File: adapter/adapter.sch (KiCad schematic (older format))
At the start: 6 parts, among them J1 Conn_01x04_Male, J2 RJ45, J3 Conn_01x02_Male

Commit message: Add some adapter and interconnect pics
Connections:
- net GND: now also J1.4 (Pin_4); no longer J1.1 (Pin_1)
- net A: now reaches J1.2 (Pin_2), J2.1
- net B: now reaches J1.3 (Pin_3), J2.2
- net A/GND: now reaches J2.7, JP2.1 (A)
- net B/VCC: now reaches J2.8, JP1.1 (A)
- net at JP3.1 (A): now also J1.1 (Pin_1); no longer J1.4 (Pin_4)
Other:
- moved on the sheet: J2, JP3
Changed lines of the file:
@@
 Comment9 ""
 $EndDescr
-Wire Wire Line
-	3550 4700 5275 4700
-Wire Wire Line
-	4625 4300 3550 4300
-Wire Wire Line
-	4525 4600 3550 4600
-Wire Wire Line
-	4625 4500 3550 4500
+Connection ~ 4175 4400
+Connection ~ 4525 4600
+Connection ~ 4625 3975
+Connection ~ 4625 4300
+Wire Wire Line
+	2750 4100 3775 4100
+Wire Wire Line
+	2750 4200 3775 4200
+Wire Wire Line
+	2750 4700 5275 4700
+Wire Wire Line
+	2750 4800 5375 4800
+Wire Wire Line
+	3775 4100 3775 3975
+Wire Wire Line
+	3975 3075 5200 3075
+Wire Wire Line
+	4175 3975 4625 3975
+Wire Wire Line
+	4175 4200 4175 4400
+Wire Wire Line
+	4175 4400 2750 4400
 Wire Wire Line
 	4525 4400 4175 4400
 Wire Wire Line
-	5200 4250 5850 4250
+	4525 4400 4525 4600
+Wire Wire Line
+	4525 4600 2750 4600
+Wire Wire Line
+	4525 4600 4525 4875
+Wire Wire Line
+	4625 3975 4625 4300
+Wire Wire Line
+	4625 4300 2750 4300
+Wire Wire Line
+	4625 4300 4625 4500
+Wire Wire Line
+	4625 4300 5050 4300
+Wire Wire Line
+	4625 4500 2750 4500
+Wire Wire Line
+	5050 4300 5050 3800
+Wire Wire Line
+	5200 3075 5200 3550
+Wire Wire Line
+	5200 4050 5750 4050
+Wire Wire Line
+	5275 4350 5850 4350
+Wire Wire Line
+	5275 4700 5275 4350
+Wire Wire Line
+	5375 4450 5850 4450
 Wire Wire Line
 	5375 4800 5375 4450
 Wire Wire Line
-	5375 4450 5850 4450
-Wire Wire Line
-	5275 4350 5850 4350
-Wire Wire Line
-	5275 4700 5275 4350
+	5650 4250 5650 4550
+Wire Wire Line
+	5750 4050 5750 4550
+Wire Wire Line
+	5750 4550 5850 4550
+Wire Wire Line
+	5850 4250 5650 4250
+Text Notes 2925 4300 2    50   ~ 0
+O
+Text Notes 2925 4400 2    50   ~ 0
+BW
+Text Notes 2925 4500 2    50   ~ 0
+B
+Text Notes 2925 4600 2    50   ~ 0
+OW
+Text Notes 2925 4700 2    50   ~ 0
+G
+Text Notes 2950 4100 2    50   ~ 0
+BR
+Text Notes 2950 4200 2    50   ~ 0
+BRW
+Text Notes 2950 4800 2    50   ~ 0
+GW
+Text Label 3125 4300 2    50   ~ 0
+VCC
+Text Label 3125 4400 2    50   ~ 0
+GND
+Text Label 3125 4500 2    50   ~ 0
+VCC
+Text Label 3125 4600 2    50   ~ 0
+GND
+Text Label 3125 4700 2    50   ~ 0
+B
+Text Label 3125 4800 2    50   ~ 0
+A
+Text Label 3250 4100 2    50   ~ 0
+B{slash}VCC
+Text Label 3250 4200 2    50   ~ 0
+A{slash}GND
+Text Label 5550 4350 2    50   ~ 0
+B
+Text Label 5550 4450 2    50   ~ 0
+A
+$Comp
+L power:VCC #PWR?
+U 1 1 5E309DAF
+P 4625 3975
+F 0 "#PWR?" H 4625 3825 50  0001 C CNN
+F 1 "VCC" H 4640 4148 50  0000 C CNN
+F 2 "" H 4625 3975 50  0001 C CNN
+F 3 "" H 4625 3975 50  0001 C CNN
+	1    4625 3975
+	1    0    0    -1
+$EndComp
+$Comp
+L power:GND #PWR?
+U 1 1 5E310096
+P 3975 3175
+F 0 "#PWR?" H 3975 2925 50  0001 C CNN
+F 1 "GND" H 3980 3002 50  0000 C CNN
+F 2 "" H 3975 3175 50  0001 C CNN
+F 3 "" H 3975 3175 50  0001 C CNN
+	1    3975 3175
+	1    0    0    -1
+$EndComp
+$Comp
+L power:GND #PWR?
+U 1 1 5E30A136
+P 4525 4875
+F 0 "#PWR?" H 4525 4625 50  0001 C CNN
+F 1 "GND" H 4530 4702 50  0000 C CNN
+F 2 "" H 4525 4875 50  0001 C CNN
+F 3 "" H 4525 4875 50  0001 C CNN
+	1    4525 4875
+	1    0    0    -1
+$EndComp
+$Comp
+L power:GND #PWR?
+U 1 1 5E30BC3A
+P 5650 4550
+F 0 "#PWR?" H 5650 4300 50  0001 C CNN
+F 1 "GND" H 5655 4377 50  0000 C CNN
+F 2 "" H 5650 4550 50  0001 C CNN
+F 3 "" H 5650 4550 50  0001 C CNN
+	1    5650 4550
+	1    0    0    -1
+$EndComp
+$Comp
+L Connector:Conn_01x02_Male J3
+U 1 1 5E30CE36
+P 3775 3075
+F 0 "J3" H 3883 3254 50  0000 C CNN
+F 1 "Conn_01x02_Male" H 3883 3163 50  0000 C CNN
+F 2 "TerminalBlock_RND:TerminalBlock_RND_205-00287_Pitch5.08mm" H 3775 3075 50  0001 C CNN
+F 3 "~" H 3775 3075 50  0001 C CNN
+	1    3775 3075
+	1    0    0    -1
+$EndComp
+$Comp
+L Jumper:Jumper_2_Open JP1
+U 1 1 5E3170CB
+P 3975 3975
+F 0 "JP1" H 3975 4100 50  0000 C CNN
+F 1 "Jumper_2_Open" H 3975 4118 50  0001 C CNN
+F 2 "Jumper:SolderJumper-2_P1.3mm_Open_Pad1.0x1.5mm" H 3975 3975 50  0001 C CNN
+F 3 "~" H 3975 3975 50  0001 C CNN
+	1    3975 3975
+	1    0    0    -1
+$EndComp
+$Comp
+L Jumper:Jumper_2_Open JP2
+U 1 1 5E319375
+P 3975 4200
+F 0 "JP2" H 3975 4325 50  0000 C CNN
+F 1 "Jumper_2_Open" H 3975 4343 50  0001 C CNN
+F 2 "Jumper:SolderJumper-2_P1.3mm_Open_Pad1.0x1.5mm" H 3975 4200 50  0001 C CNN
+F 3 "~" H 3975 4200 50  0001 C CNN
+	1    3975 4200
+	1    0    0    -1
+$EndComp
 $Comp
 L Connector:Conn_01x04_Male J1
@@
 $EndComp
 $Comp
-L power:GND #PWR?
-U 1 1 5E30BC3A
-P 5850 4550
-F 0 "#PWR?" H 5850 4300 50  0001 C CNN
-F 1 "GND" H 5855 4377 50  0000 C CNN
-F 2 "" H 5850 4550 50  0001 C CNN
-F 3 "" H 5850 4550 50  0001 C CNN
-	1    5850 4550
-	1    0    0    -1
-$EndComp
-Connection ~ 4525 4600
-Wire Wire Line
-	4525 4400 4525 4600
-Wire Wire Line
-	4625 4300 4625 4500
-Connection ~ 4625 4300
-Connection ~ 4625 3975
-$Comp
 L Jumper:Jumper_3_Bridged12 JP3
 U 1 1 5E312537
-P 5200 4000
-F 0 "JP3" V 5200 4125 50  0000 C CNN
-F 1 "Jumper_3_Bridged12" H 5200 4112 50  0001 C CNN
-F 2 "Jumper:SolderJumper-3_P1.3mm_Bridged12_RoundedPad1.0x1.5mm_NumberLabels" H 5200 4000 50  0001 C CNN
-F 3 "~" H 5200 4000 50  0001 C CNN
-	1    5200 4000
+P 5200 3800
+F 0 "JP3" V 5200 3925 50  0000 C CNN
+F 1 "Jumper_3_Bridged12" H 5200 3912 50  0001 C CNN
+F 2 "Jumper:SolderJumper-3_P1.3mm_Bridged12_RoundedPad1.0x1.5mm_NumberLabels" H 5200 3800 50  0001 C CNN
+F 3 "~" H 5200 3800 50  0001 C CNN
+	1    5200 3800
 	0    1    -1   0
 $EndComp
-Wire Wire Line
-	4625 3975 4625 4300
-Wire Wire Line
-	5200 3075 5200 3750
-Wire Wire Line
-	4625 4300 5050 4300
-Wire Wire Line
-	5050 4300 5050 4000
-Wire Wire Line
-	3975 3075 5200 3075
-Text Notes 3700 4700 2    50   ~ 0
-G
-Text Notes 3700 4600 2    50   ~ 0
-OW
-Text Notes 3700 4500 2    50   ~ 0
-B
-Text Notes 3700 4400 2    50   ~ 0
-BW
-Wire Wire Line
-	3550 4200 3775 4200
-Wire Wire Line
-	4175 4400 3550 4400
-Wire Wire Line
-	4175 4200 4175 4400
-Text Notes 3700 4300 2    50   ~ 0
-O
-Text Notes 3725 4200 2    50   ~ 0
-BRW
-Text Notes 3725 4100 2    50   ~ 0
-BR
-Text Notes 3725 4800 2    50   ~ 0
-GW
-Wire Wire Line
-	3550 4100 3775 4100
-Wire Wire Line
-	3775 4100 3775 3975
 $Comp
 L Connector:RJ45 J2
 U 1 1 5E263AF8
-P 3150 4500
-F 0 "J2" H 3207 5166 50  0000 C CNN
-F 1 "RJ45" H 3207 5075 50  0000 C CNN
-F 2 "Connector_RJ:RJ45_Amphenol_54602-x08_Horizontal" V 3150 4525 50  0001 C CNN
-F 3 "~" V 3150 4525 50  0001 C CNN
-	1    3150 4500
-	1    0    0    -1
-$EndComp
-Wire Wire Line
-	4175 3975 4625 3975
-$Comp
-L Connector:Conn_01x02_Male J3
-U 1 1 5E30CE36
-P 3775 3075
-F 0 "J3" H 3883 3254 50  0000 C CNN
-F 1 "Conn_01x02_Male" H 3883 3163 50  0000 C CNN
-F 2 "TerminalBlock_RND:TerminalBlock_RND_205-00287_Pitch5.08mm" H 3775 3075 50  0001 C CNN
-F 3 "~" H 3775 3075 50  0001 C CNN
-	1    3775 3075
-	1    0    0    -1
-$EndComp
-$Comp
-L Jumper:Jumper_2_Open JP1
-U 1 1 5E3170CB
-P 3975 3975
-F 0 "JP1" H 3975 4100 50  0000 C CNN
-F 1 "Jumper_2_Open" H 3975 4118 50  0001 C CNN
-F 2 "Jumper:SolderJumper-2_P1.3mm_Open_Pad1.0x1.5mm" H 3975 3975 50  0001 C CNN
-F 3 "~" H 3975 3975 50  0001 C CNN
-	1    3975 3975
-	1    0    0    -1
-$EndComp
-$Comp
-L Jumper:Jumper_2_Open JP2
-U 1 1 5E319375
-P 3975 4200
-F 0 "JP2" H 3975 4325 50  0000 C CNN
-F 1 "Jumper_2_Open" H 3975 4343 50  0001 C CNN
-F 2 "Jumper:SolderJumper-2_P1.3mm_Open_Pad1.0x1.5mm" H 3975 4200 50  0001 C CNN
-F 3 "~" H 3975 4200 50  0001 C CNN
-	1    3975 4200
-	1    0    0    -1
-$EndComp
-$Comp
-L power:GND #PWR?
-U 1 1 5E310096
-P 3975 3175
-F 0 "#PWR?" H 3975 2925 50  0001 C CNN
-F 1 "GND" H 3980 3002 50  0000 C CNN
-F 2 "" H 3975 3175 50  0001 C CNN
-F 3 "" H 3975 3175 50  0001 C CNN
-	1    3975 3175
-	1    0    0    -1
-$EndComp
-$Comp
-L power:VCC #PWR?
-U 1 1 5E309DAF
-P 4625 3975
-F 0 "#PWR?" H 4625 3825 50  0001 C CNN
-F 1 "VCC" H 4640 4148 50  0000 C CNN
-F 2 "" H 4625 3975 50  0001 C CNN
-F 3 "" H 4625 3975 50  0001 C CNN
-	1    4625 3975
-	1    0    0    -1
-$EndComp
-Connection ~ 4175 4400
-Wire Wire Line
-	3550 4800 5375 4800
-Wire Wire Line
-	4525 4600 4525 4875
-$Comp
-L power:GND #PWR?
-U 1 1 5E30A136
-P 4525 4875
-F 0 "#PWR?" H 4525 4625 50  0001 C CNN
-F 1 "GND" H 4530 4702 50  0000 C CNN
-F 2 "" H 4525 4875 50  0001 C CNN
-F 3 "" H 4525 4875 50  0001 C CNN
-	1    4525 4875
-	1    0    0    -1
-$EndComp
+P 2350 4500
+F 0 "J2" H 2407 5166 50  0000 C CNN
+F 1 "RJ45" H 2407 5075 50  0000 C CNN
+F 2 "Connector_RJ:RJ45_Amphenol_54602-x08_Horizontal" V 2350 4525 50  0001 C CNN
+F 3 "~" V 2350 4525 50  0001 C CNN
+	1    2350 4500
+	1    0    0    -1
+$EndComp

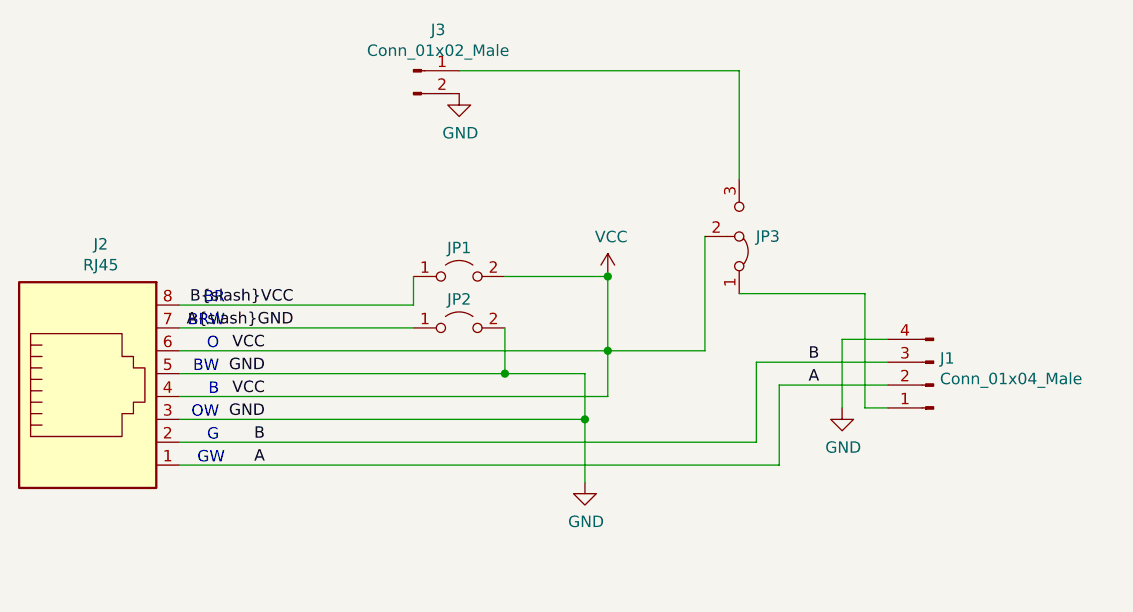
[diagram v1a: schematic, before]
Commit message: Add cable marker link
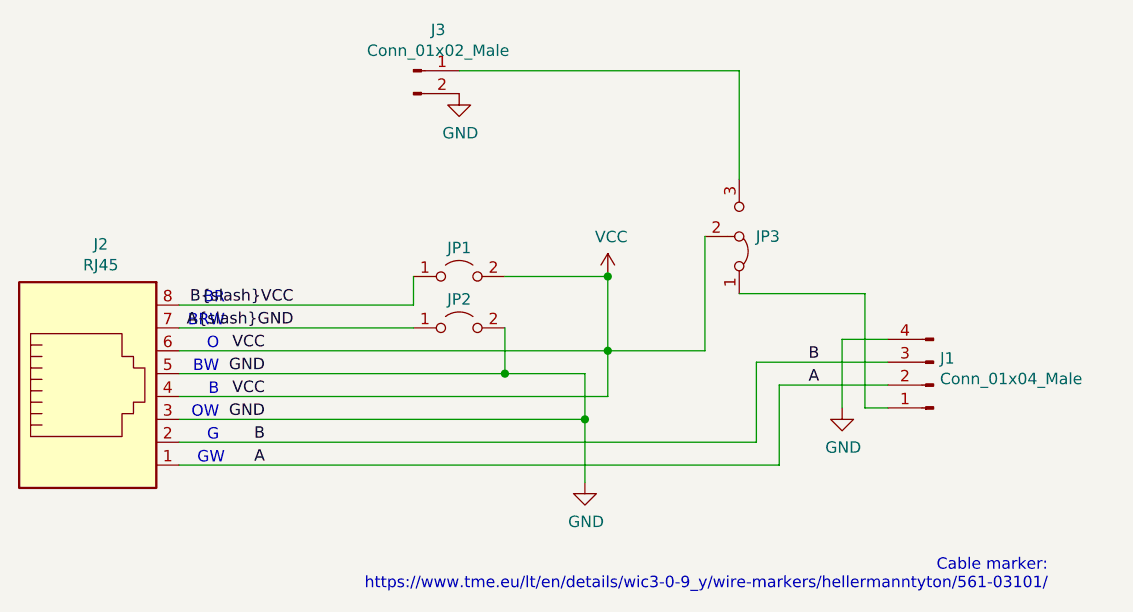
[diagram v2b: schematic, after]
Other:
- note added: "Cable marker:\nhttps://www.tme.eu/lt/en/details/wic3-0-9_y/wire-markers/hellermanntyton/561-03101/"
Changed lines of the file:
@@
 EESchema Schematic File Version 5
-EELAYER 30 0
+EELAYER 33 0
 EELAYER END
 $Descr A4 11693 8268
@@
 Text Notes 2950 4800 2    50   ~ 0
 GW
+Text Notes 6550 5350 2    50   ~ 0
+Cable marker:\nhttps://www.tme.eu/lt/en/details/wic3-0-9_y/wire-markers/hellermanntyton/561-03101/
 Text Label 3125 4300 2    50   ~ 0
 VCC
